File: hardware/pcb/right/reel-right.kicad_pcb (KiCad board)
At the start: 2 copper layers, 147.7 x 92.6 mm, 47 parts, among them J1 Conn_01x02, J3 Conn_01x05, SW1 SW_Push, SW10 SW_Push, SW11 SW_Push, SW12 SW_Push, SW13 SW_Push, SW14 SW_Push, SW15 SW_Push, SW16 SW_Push, SW17 SW_Push, SW18 SW_Push, SW19 SW_Push, SW2 SW_Push, SW22 SW_SPDT, SW3 SW_Push, SW4 SW_Push, SW5 SW_Push, SW6 SW_Push, SW7 SW_Push, SW8 SW_Push, SW9 SW_Push

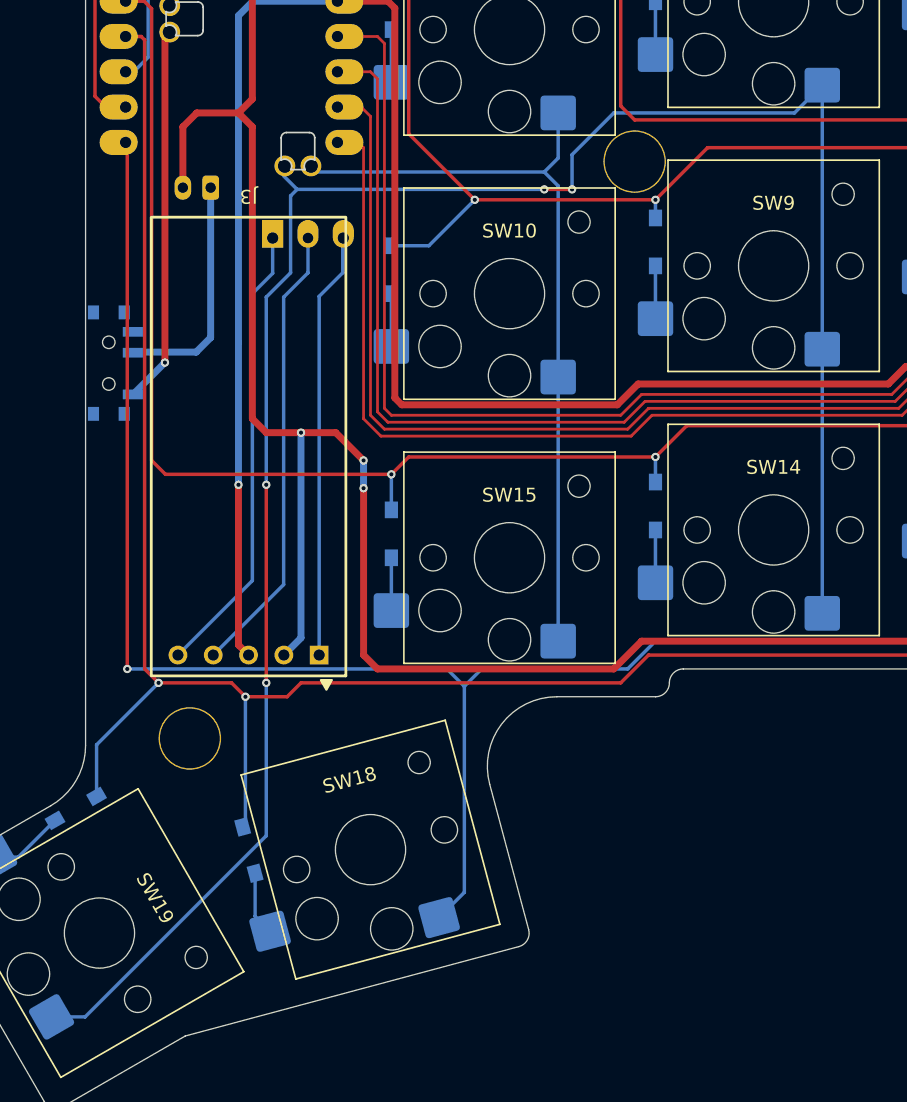
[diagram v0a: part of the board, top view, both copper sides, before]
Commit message: Update left and right PCB routing
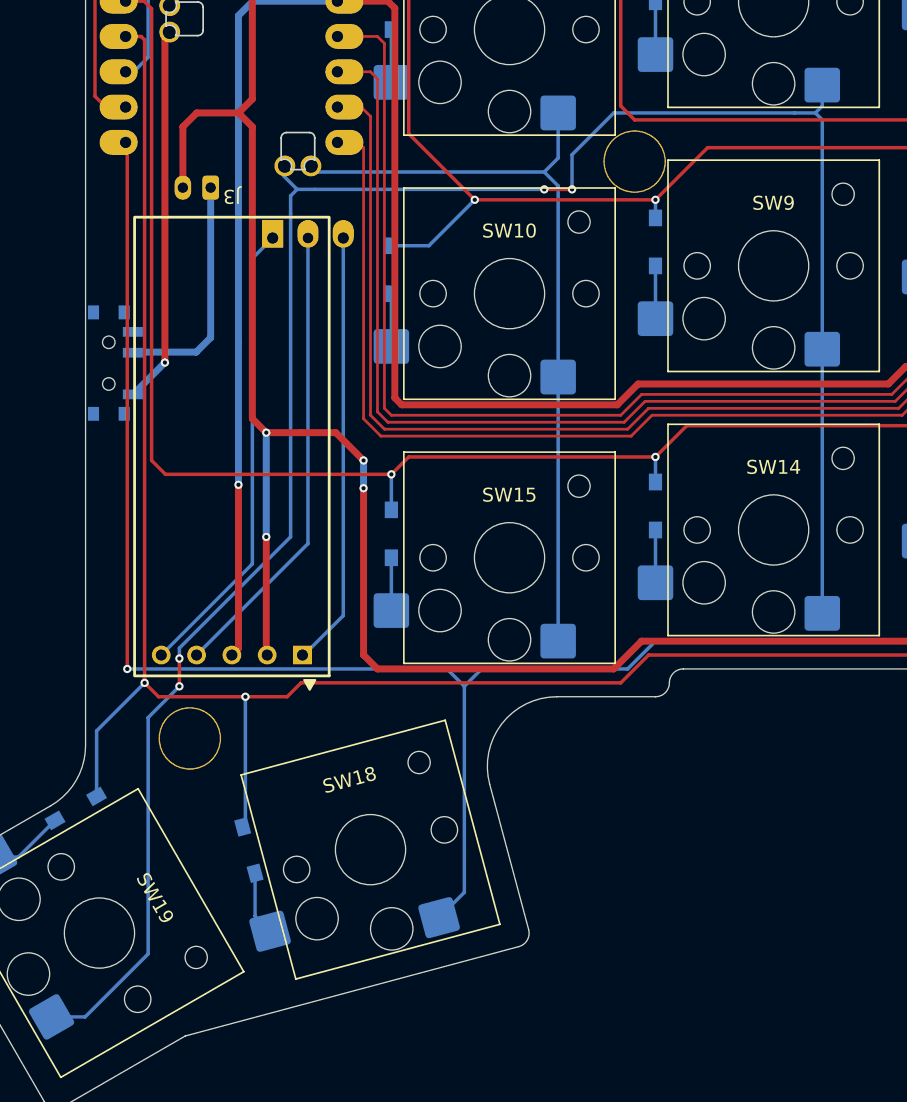
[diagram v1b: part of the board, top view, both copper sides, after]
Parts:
- moved J3 1.20 mm to (59.0, 103.5)
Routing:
- net CS: track 30.7 -> 31.3 mm
- net GND: track 185.9 -> 185.5 mm, vias 4 -> 5
